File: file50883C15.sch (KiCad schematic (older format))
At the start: 11 parts

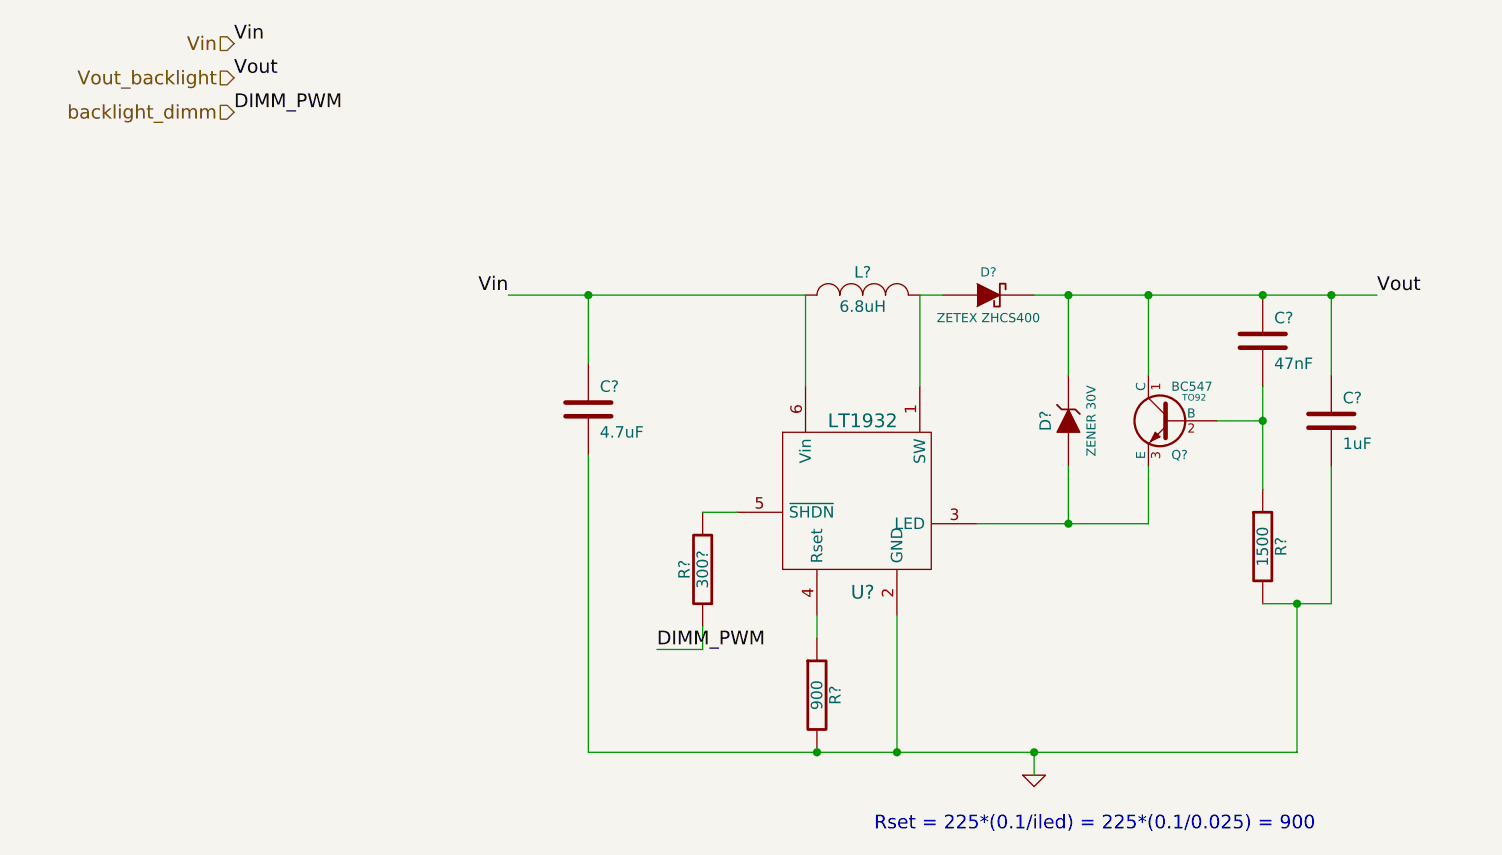
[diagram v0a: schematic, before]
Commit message: Added power supply
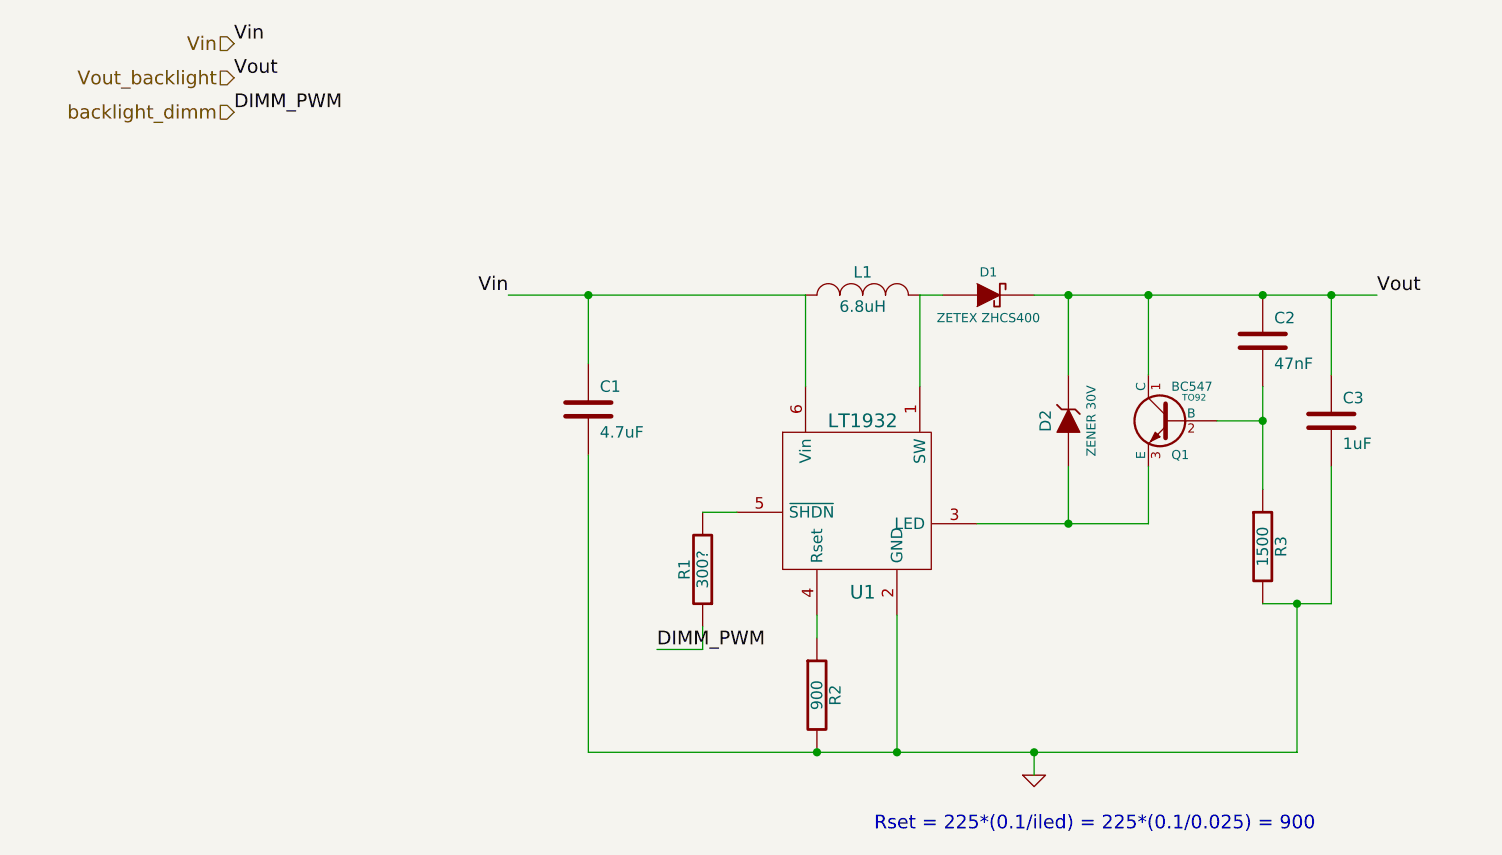
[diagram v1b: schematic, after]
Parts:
- gave numbers to parts that had none: 11
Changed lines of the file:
@@
-EESchema Schematic File Version 2  date Fri 26 Oct 2012 14:46:37 CEST
+EESchema Schematic File Version 2  date Sun 28 Oct 2012 15:35:36 CET
 LIBS:power
 LIBS:device
@@
 Sheet 2 3
 Title "LCD backlight driver"
-Date "26 oct 2012"
+Date "28 oct 2012"
 Rev "0.1"
 Comp ""
@@
 $EndDescr
 $Comp
-L LT1932 U?
+L LT1932 U1
 U 1 1 508849D1
 P 4200 3300
-F 0 "U?" H 4200 2900 60  0000 C CNN
+F 0 "U1" H 4200 2900 60  0000 C CNN
 F 1 "LT1932" H 4200 3650 60  0000 C CNN
 	1    4200 3300
@@
 $EndComp
 $Comp
-L INDUCTOR_SMALL L?
+L INDUCTOR_SMALL L1
 U 1 1 508849E0
 P 4200 2400
-F 0 "L?" H 4200 2500 50  0000 C CNN
+F 0 "L1" H 4200 2500 50  0000 C CNN
 F 1 "6.8uH" H 4200 2350 50  0000 C CNN
 	1    4200 2400
@@
 $EndComp
 $Comp
-L DIODESCH D?
+L DIODESCH D1
 U 1 1 508849EF
 P 4750 2400
-F 0 "D?" H 4750 2500 40  0000 C CNN
+F 0 "D1" H 4750 2500 40  0000 C CNN
 F 1 "ZETEX ZHCS400" H 4750 2300 40  0000 C CNN
 	1    4750 2400
@@
 $EndComp
 $Comp
-L C C?
+L C C3
 U 1 1 508849FE
 P 6250 2950
-F 0 "C?" H 6300 3050 50  0000 L CNN
+F 0 "C3" H 6300 3050 50  0000 L CNN
 F 1 "1uF" H 6300 2850 50  0000 L CNN
 	1    6250 2950
@@
 $EndComp
 $Comp
-L C C?
+L C C1
 U 1 1 50884A0D
 P 3000 2900
-F 0 "C?" H 3050 3000 50  0000 L CNN
+F 0 "C1" H 3050 3000 50  0000 L CNN
 F 1 "4.7uF" H 3050 2800 50  0000 L CNN
 	1    3000 2900
@@
 $EndComp
 $Comp
-L R R?
+L R R2
 U 1 1 50884A1C
 P 4000 4150
-F 0 "R?" V 4080 4150 50  0000 C CNN
+F 0 "R2" V 4080 4150 50  0000 C CNN
 F 1 "900" V 4000 4150 50  0000 C CNN
 	1    4000 4150
@@
 Rset = 225*(0.1/iled) = 225*(0.1/0.025) = 900
 $Comp
-L ZENER D?
+L ZENER D2
 U 1 1 50884C55
 P 5100 2950
-F 0 "D?" H 5100 3050 50  0000 C CNN
+F 0 "D2" H 5100 3050 50  0000 C CNN
 F 1 "ZENER 30V" H 5100 2850 40  0000 C CNN
 	1    5100 2950
@@
 $EndComp
 $Comp
-L BC547 Q?
+L BC547 Q1
 U 1 1 50884CAA
 P 5550 2950
-F 0 "Q?" H 5550 2801 40  0000 R CNN
+F 0 "Q1" H 5550 2801 40  0000 R CNN
 F 1 "BC547" H 5550 3100 40  0000 R CNN
 F 2 "TO92" H 5450 3052 29  0000 C CNN
@@
 $EndComp
 $Comp
-L R R?
+L R R3
 U 1 1 50884CB9
 P 5950 3500
-F 0 "R?" V 6030 3500 50  0000 C CNN
+F 0 "R3" V 6030 3500 50  0000 C CNN
 F 1 "1500" V 5950 3500 50  0000 C CNN
 	1    5950 3500
@@
 $EndComp
 $Comp
-L C C?
+L C C2
 U 1 1 50884CD2
 P 5950 2600
-F 0 "C?" H 6000 2700 50  0000 L CNN
+F 0 "C2" H 6000 2700 50  0000 L CNN
 F 1 "47nF" H 6000 2500 50  0000 L CNN
 	1    5950 2600
@@
 Connection ~ 4950 4400
 $Comp
-L GND #PWR?
+L GND #PWR07
 U 1 1 50884EBB
 P 4950 4500
-F 0 "#PWR?" H 4950 4500 30  0001 C CNN
+F 0 "#PWR07" H 4950 4500 30  0001 C CNN
 F 1 "GND" H 4950 4430 30  0001 C CNN
 	1    4950 4500
@@
 Connection ~ 4000 4400
 $Comp
-L R R?
+L R R1
 U 1 1 508851BA
 P 3500 3600
-F 0 "R?" V 3580 3600 50  0000 C CNN
+F 0 "R1" V 3580 3600 50  0000 C CNN
 F 1 "300?" V 3500 3600 50  0000 C CNN
 	1    3500 3600

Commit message: lots of changes
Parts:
- R1: value 300? -> 300
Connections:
- net Vout-: now reaches D2.1 (A), Q1.3 (E), U1.3 (LED)
- net Vout_backlight renamed Vout
- net backlight_dimm renamed dimm
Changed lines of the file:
@@
-EESchema Schematic File Version 2  date Thu 01 Nov 2012 14:43:35 CET
+EESchema Schematic File Version 2  date Thu 08 Nov 2012 00:17:25 CET
 LIBS:power
 LIBS:device
@@
 Sheet 2 4
 Title "LCD backlight driver"
-Date "1 nov 2012"
+Date "7 nov 2012"
 Rev "0.1"
 Comp ""
@@
 P 3500 3600
 F 0 "R1" V 3580 3600 50  0000 C CNN
-F 1 "300?" V 3500 3600 50  0000 C CNN
+F 1 "300" V 3500 3600 50  0000 C CNN
 	1    3500 3600
 	-1   0    0    1
@@
 Wire Wire Line
 	3500 3350 3650 3350
-Wire Wire Line
-	3500 3850 3500 3950
-Wire Wire Line
-	3500 3950 3300 3950
-Text Label 3300 3950 0    60   ~ 0
-DIMM_PWM
 Connection ~ 3000 2400
 Text Label 2650 2400 2    60   ~ 0
 Vin
 Connection ~ 6250 2400
-Text Label 6450 2400 0    60   ~ 0
-Vout
 Text HLabel 1450 1300 0    60   Input ~ 0
 Vin
-Text HLabel 1450 1450 0    60   Input ~ 0
-Vout_backlight
-Text HLabel 1450 1600 0    60   Input ~ 0
-backlight_dimm
-Text Label 1450 1600 0    60   ~ 0
-DIMM_PWM
 Text Label 1450 1300 0    60   ~ 0
 Vin
-Text Label 1450 1450 0    60   ~ 0
+Connection ~ 6250 2750
+Connection ~ 6250 3150
+Connection ~ 5950 3750
+Connection ~ 5950 3250
+Connection ~ 5750 2950
+Connection ~ 5450 2750
+Connection ~ 5450 3150
+Connection ~ 4950 2400
+Connection ~ 4550 2400
+Text HLabel 6450 2400 2    60   Input ~ 0
 Vout
+Wire Wire Line
+	3500 3850 3550 3850
+Wire Wire Line
+	3550 3850 3550 3950
+Wire Wire Line
+	3550 3950 3500 3950
+Text HLabel 3500 3950 0    60   Input ~ 0
+dimm
+Connection ~ 3500 3850
+Text HLabel 5450 3400 2    60   Input ~ 0
+Vout-
 $EndSCHEMATC
